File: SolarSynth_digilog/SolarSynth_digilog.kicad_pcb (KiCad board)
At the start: 2 copper layers, 59.9 x 90 mm, 31 parts, among them J1 OutputJack1, J2 Conn_01x01_Pin, J3 Conn_01x01_Pin, P1 PiezoDisc, P2 PiezoDisc, U1 74HC14, U2 MCP6002-xMC

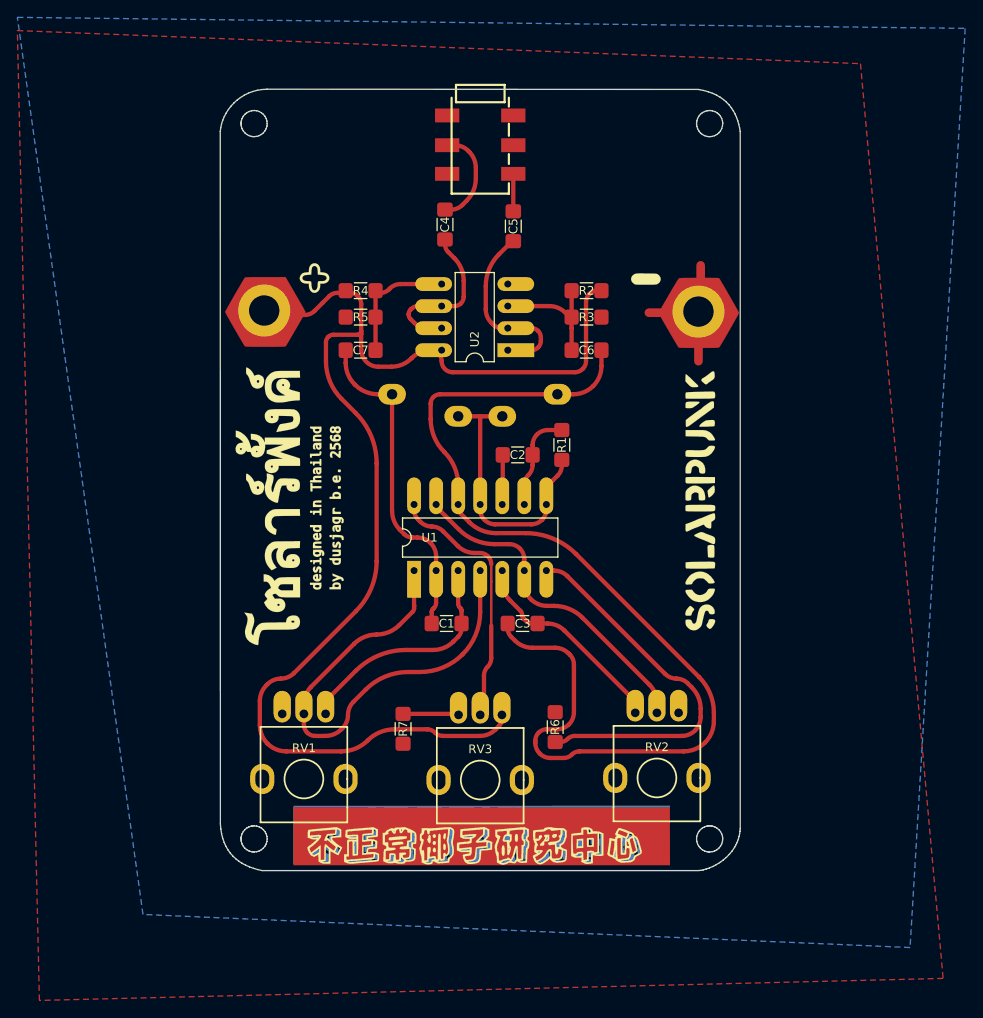
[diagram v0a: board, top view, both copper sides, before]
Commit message: Update KiCad project files and add 3D models
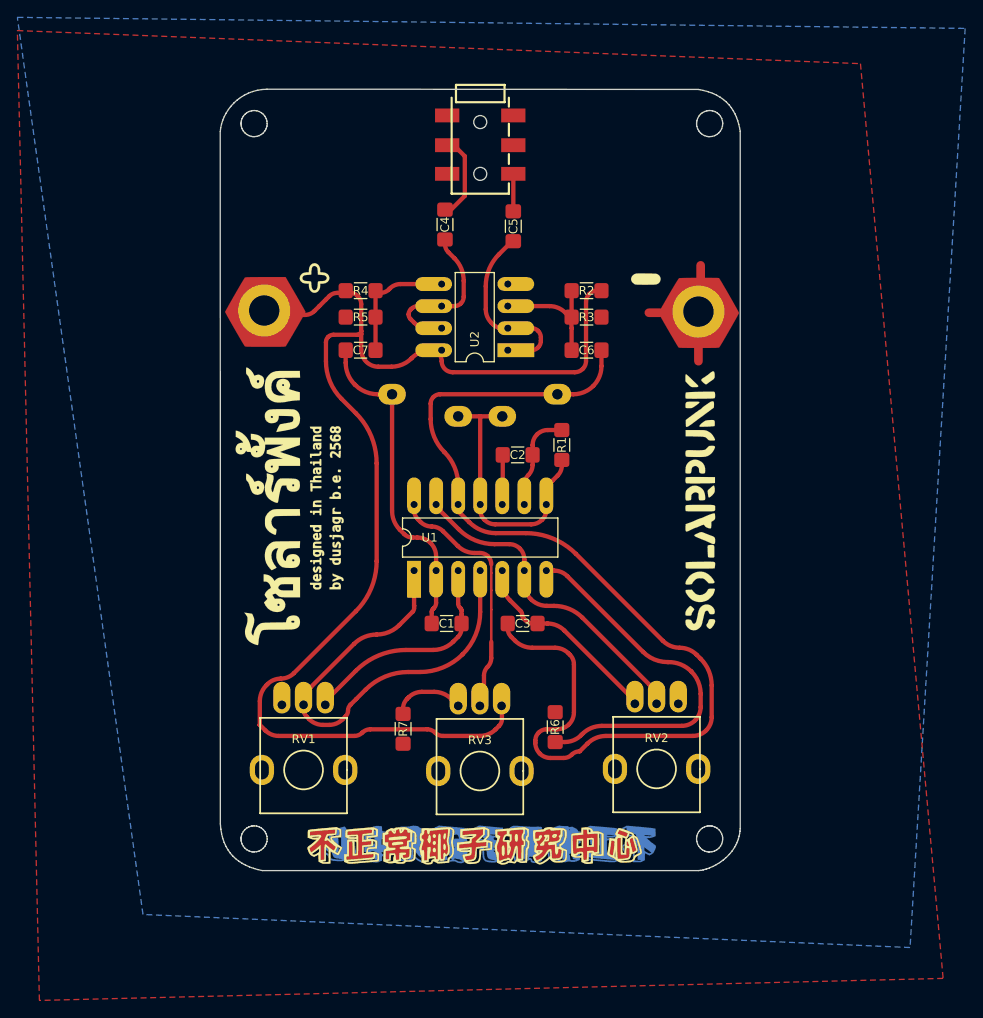
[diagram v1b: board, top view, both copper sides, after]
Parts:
- J1: footprint 007_dusjagr:AUDIO-JACK-3.5mm_SMD_noHole -> 007_dusjagr:AUDIO-JACK-3.5mm_SMD_Hole
- moved RV2 1.04 mm to (137.2, 107.9)
- moved RV3 1.04 mm to (116.8, 108.2)
- moved RV1 1.04 mm to (96.5, 108.1)
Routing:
- net Net-(RV1-Pad2): track 57.4 -> 55.0 mm
- net Net-(R7-Pad1): track 6.43 -> 8.51 mm
- net VCC: track 142.6 -> 140.9 mm
- net Net-(RV2-Pad2): track 38.5 -> 37.3 mm
- net Net-(U1G-VCC): track 30.0 -> 29.1 mm
- net Net-(C1-Pad2): track 27.0 -> 26.2 mm
- net Net-(C4-Pad2): track 11.7 -> 11.0 mm
- net Net-(C3-Pad2): track 24.2 -> 23.5 mm

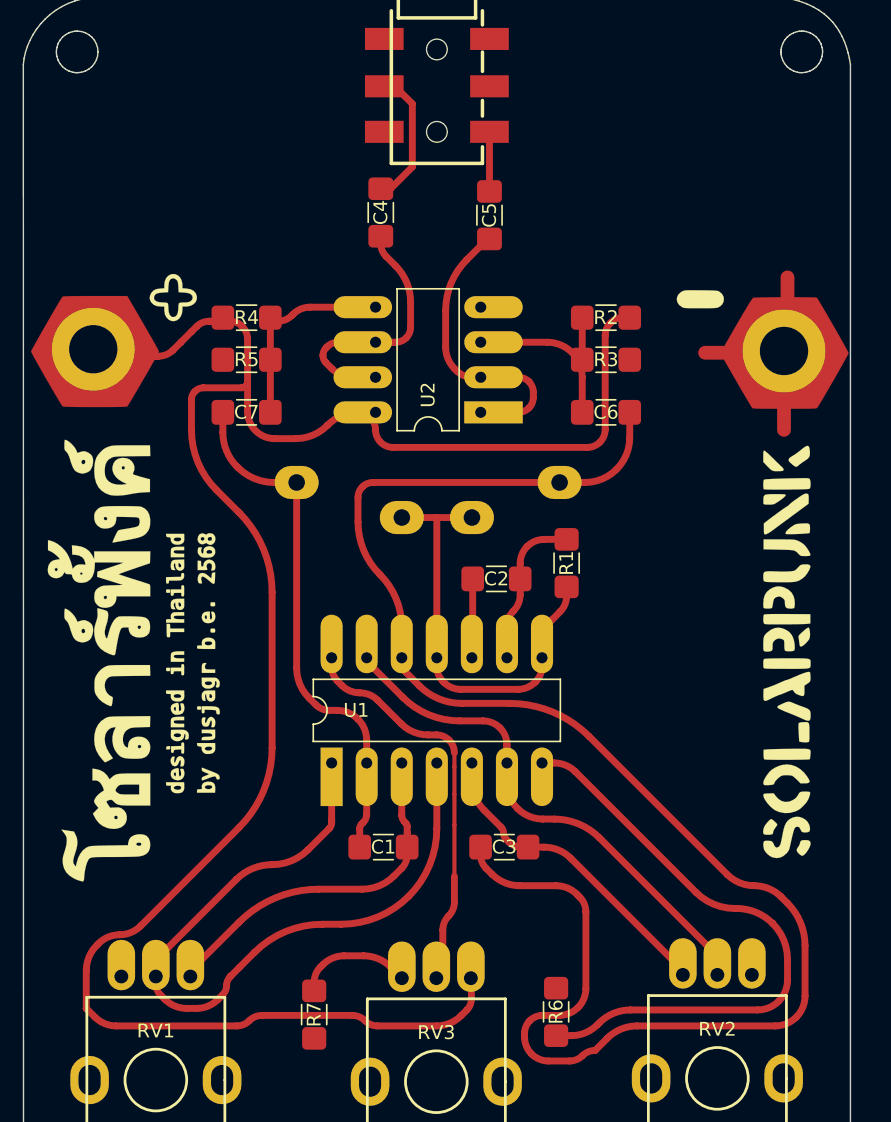
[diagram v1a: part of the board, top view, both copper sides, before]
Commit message: Update documentation with detailed assembly instructions and add new resources for Digilog edition
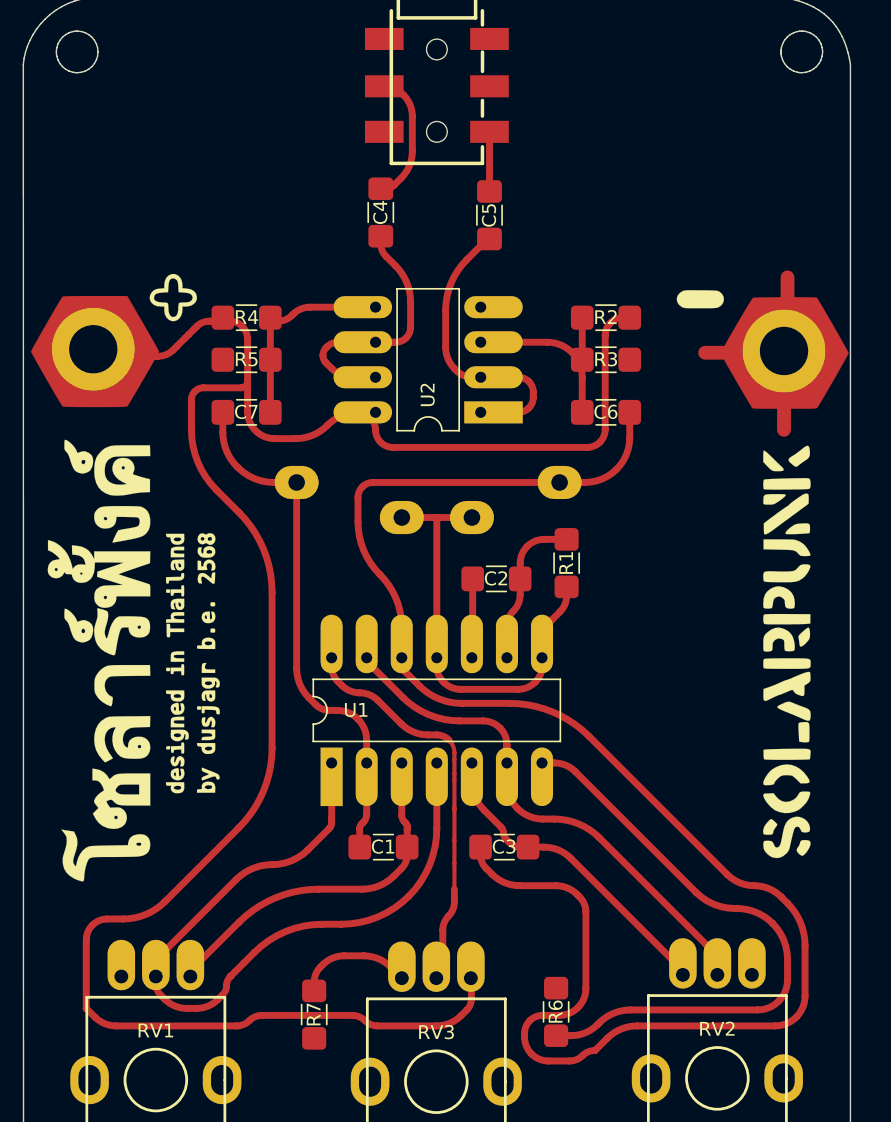
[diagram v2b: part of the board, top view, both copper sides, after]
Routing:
- net Net-(C4-Pad2): track 11.0 -> 9.88 mm
- net VCC: track 140.9 -> 141.9 mm
